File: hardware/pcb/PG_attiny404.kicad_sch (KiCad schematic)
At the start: 31 parts, among them J1 0022232041, J2 Conn_01x01_Male, J3 Conn_01x01_Male, J4 Conn_01x01_Male, J5 Conn_01x01_Male, J6 Conn_01x01_Male, J7 Conn_01x01_Male, J8 Conn_01x01_Male, J9 Conn_01x01_Male, Q1 2N7002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

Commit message: New PCB Version 0.1
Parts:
- removed C6: 100nF, Capacitor_SMD:C_0805_2012Metric_Pad1.18x1.45mm_HandSolder, symbol Device:C
- removed U2: AH9246, Package_TO_SOT_SMD:SC-59_Handsoldering, symbol project:AH9246
- added F1: 0ZCG0075FF2C, 0ZCG0075FF2C:0ZCG0075FF2C, symbol Device:Polyfuse
- added R7: 10k, Resistor_SMD:R_0805_2012Metric_Pad1.20x1.40mm_HandSolder, symbol Device:R
- added SW2: PTS526 SM15 SMTR2 LFS, PTS526_SK15_SMTR2_LFS:PTS526SK15SMTR2 LFS-M, symbol PTS526_SK15_SMTR2_LFS:PTS526_SM15_SMTR2_LFS
- added TVS1: SMF13A, SMF13A:SMFSeries_LTF, symbol SMF13A:SMF13A
- added TVS2, TVS3, TVS4: ESDA041-1JY, ESDA041-1JY:CR_041-1JY_STM, symbol ESDA041-1JY:ESDA041-1JY
- J1: footprint SOT23:PinHeader_1x04_P2.54mm_Horizontal_spezial -> digikey-footprints:PinHeader_1x4_P2.54mm_Drill1.02mm; DK_Detail_Page https://www.digikey.at/de/products/detail/molex/0022286040/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 -> /product-detail/en/molex/0022232041/WM4202-ND/26671; Description_1 (none) -> CONN HEADER VERT 4POS 2.54MM
- J2, J3, J4, J5, J6, J7, J8, J9: symbol Connector:Conn_01x01_Male -> Connector:Conn_01x01_Pin
- MOSFET1: footprint SOT23:SOT-23F_TOS-L -> SOT23:SOT-23F_TOS
- Q1: value 2N7002 -> 2N7002K-AU_R1_000A2; footprint Package_TO_SOT_SMD:SOT-323_SC-70_Handsoldering -> Package_TO_SOT_SMD:SOT-23_Handsoldering; symbol PG_attiny404-rescue:2N7002-dk_Transistors-FETs-MOSFETs-Single -> PG_attiny804:2N7002-dk_Transistors-FETs-MOSFETs-Single; DK_Detail_Page https://www.digikey.at/de/products/detail/panjit-internatio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 -> https://www.digikey.at/en/products/detail/panjit-internatio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; Description_1 (none) -> MOSFET N-CH 60V 115MA SOT-23
- R1: value 68 Ohm -> 62 Ohm
- R2: value 68 Ohm -> 100 Ohm
- U1: value ATtiny404-SS -> ATtiny804-SS; symbol PG_attiny404-rescue:ATtiny404-SS-MCU_Microchip_ATtiny -> PG_attiny804:ATtiny404-SS-MCU_Microchip_ATtiny
- U4: footprint Package_TO_SOT_SMD:SC-59_Handsoldering -> Package_TO_SOT_SMD:SOT-23_Handsoldering
- U5: footprint Package_TO_SOT_SMD:SOT-89-3_Handsoldering -> Package_TO_SOT_SMD:SOT-89-3
- U6: footprint Package_TO_SOT_SMD:SOT-23-6_Handsoldering -> Package_TO_SOT_SMD:SOT-23-6; symbol project:MP6513GJ -> PG_attiny804:MP6513GJ
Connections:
- net +3V3: now also SW2.2, TVS3.2
- net +BATT: now also TVS1.2 (K)
- net GND: now also R7.2, TVS1.1 (A), TVS2.1, TVS3.1, TVS4.1
- net Hall: now also R7.1, SW2.4
- net Soilmoisture: now also TVS2.2
- net at J5.1 (Pin_1), Q1.3 (D): now also TVS4.2
- net at J3.1 (Pin_1): now also F1.1; no longer MOSFET1.3
- new net: F1.2, MOSFET1.3
- no-connect marks 0 -> 2
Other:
- moved on the sheet: MOSFET1

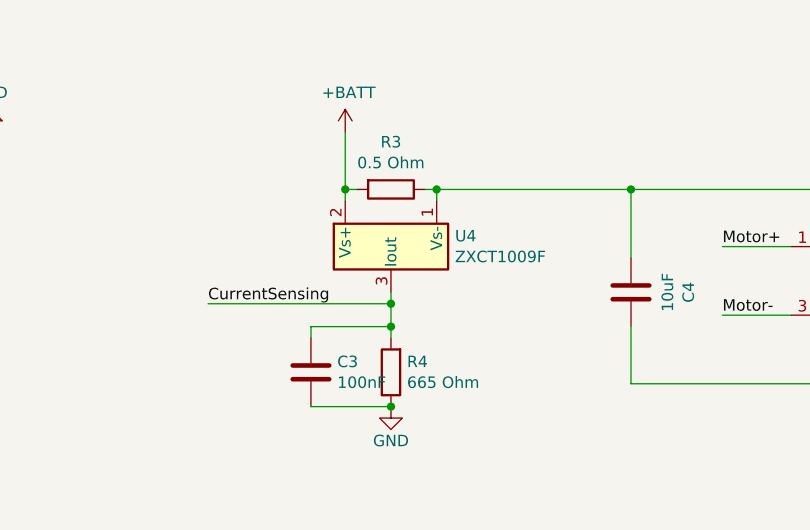
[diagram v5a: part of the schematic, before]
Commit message: Footprint correction for Current Sensor
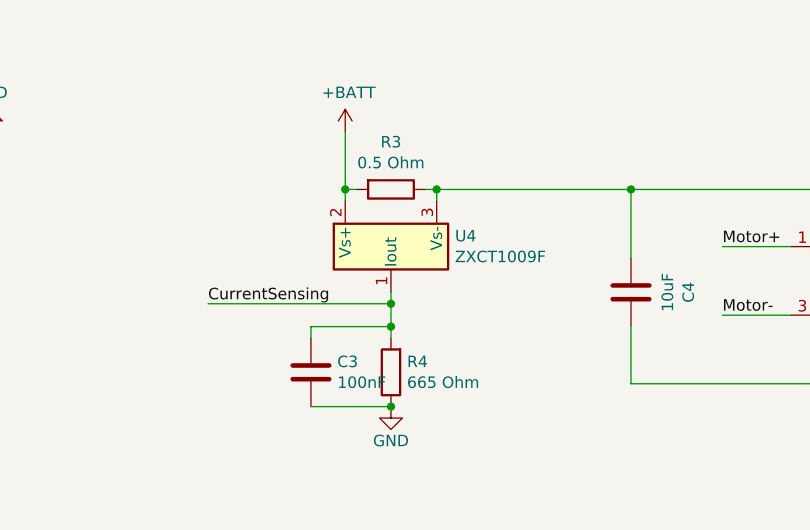
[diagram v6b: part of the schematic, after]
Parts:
- U4: footprint Package_TO_SOT_SMD:SOT-23_Handsoldering -> ZXCT1009F:SOT-23_Handsoldering_ZXCT1009F; symbol Amplifier_Current:ZXCT1009F -> ZXCT1009F:ZXCT1009F
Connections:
- net CurrentSensing: now also U4.1 (Iout); no longer U4.3 (Iout)
- net at C4.2, R3.1, U6.5 (VCC): now also U4.3 (Vs-); no longer U4.1 (Vs-)
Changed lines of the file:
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@@
 	)
 	(symbol
-		(lib_id "Amplifier_Current:ZXCT1009F")
+		(lib_id "ZXCT1009F:ZXCT1009F")
 		(at 184.15 48.26 0)
 		(unit 1)
@@
 			)
 		)
-		(property "Footprint" "Package_TO_SOT_SMD:SOT-23_Handsoldering"
+		(property "Footprint" "ZXCT1009F:SOT-23_Handsoldering_ZXCT1009F"
 			(at 184.15 48.26 0)
 			(effects

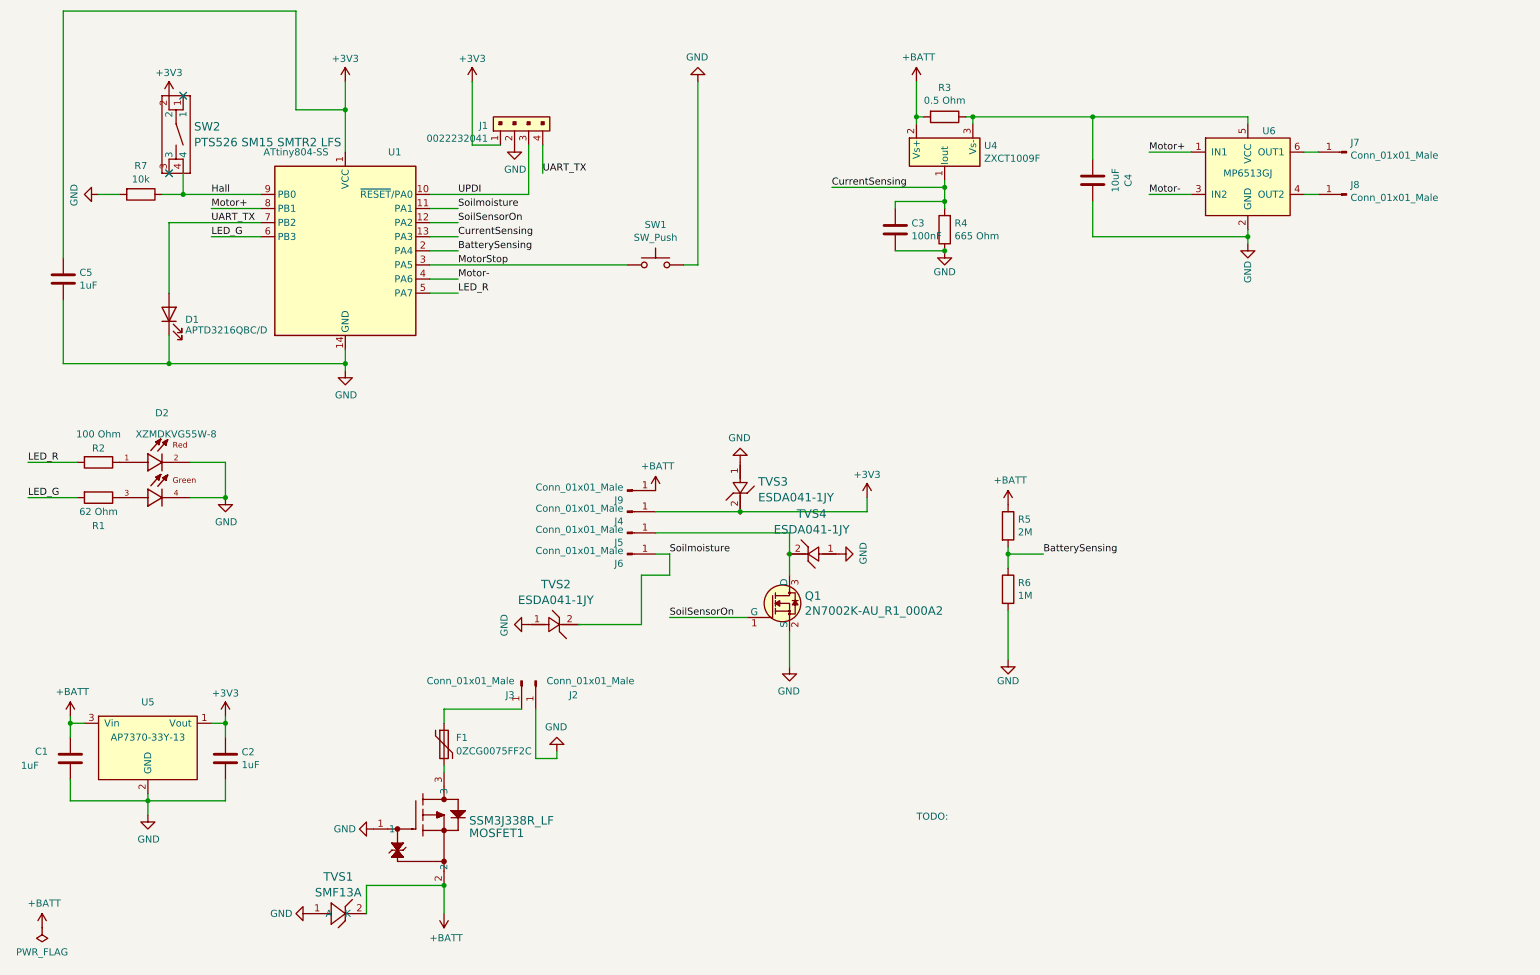
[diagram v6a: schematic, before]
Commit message: Added new motor driver to pcb
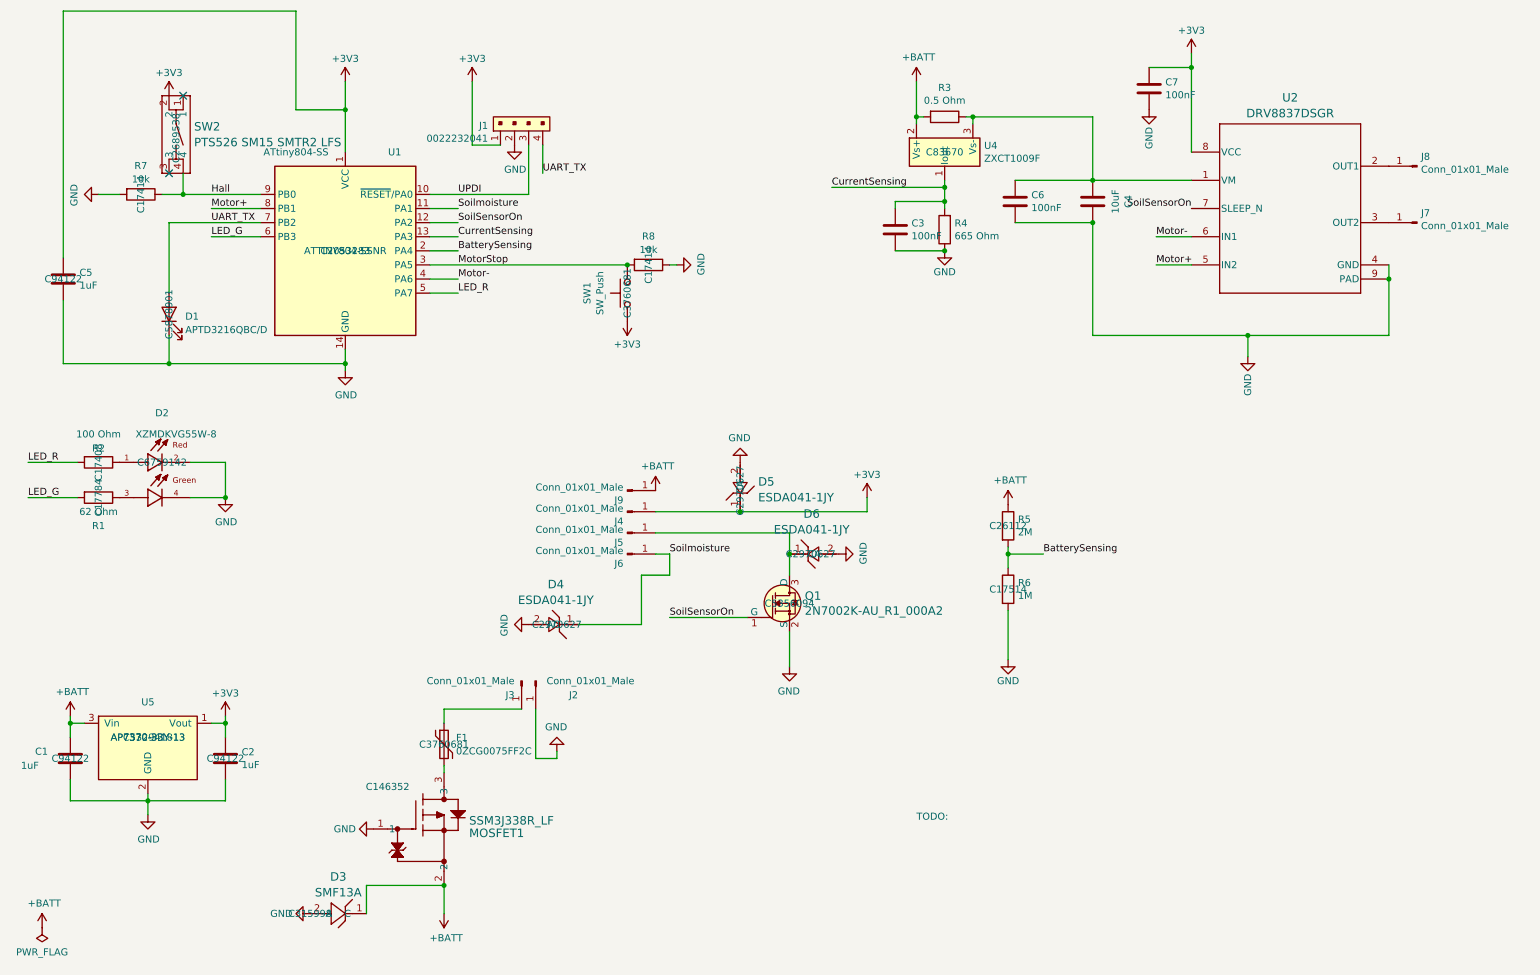
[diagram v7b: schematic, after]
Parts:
- removed U6: MP6513GJ, Package_TO_SOT_SMD:SOT-23-6, symbol PG_attiny804:MP6513GJ
- added C6, C7: 100nF, Capacitor_SMD:C_0805_2012Metric_Pad1.18x1.45mm_HandSolder, symbol Device:C
- added R8: 10k, Resistor_SMD:R_0805_2012Metric_Pad1.20x1.40mm_HandSolder, symbol Device:R
- added U2: DRV8837DSGR, DRV8837DSGR:DRV8837DSGR_NV, symbol DRV8837DSGR:DRV8837DSGR
- C1, C2, C5: JLC (none) -> C94122; MPN (none) -> CL21B105KOFNNNE
- C3: JLC (none) -> C519980; MPN (none) -> CC0805KRX7R7BB104
- C4: JLC (none) -> C326595; MPN (none) -> CL21A106KOQNNNG
- D1: JLC (none) -> C5878901; MPN (none) -> APTD3216QBC/D
- D2: JLC (none) -> C6759142; MPN (none) -> XZMDKVG55W-8
- D3: renamed from TVS1; JLC (none) -> C315998; MPN (none) -> SMF13A; Manufacturer (none) -> Littelfuse
- D4: renamed from TVS2; JLC (none) -> C2970627; MPN (none) -> ESDA041-1JY
- D5: renamed from TVS3; JLC (none) -> C2970627; MPN (none) -> ESDA041-1JY
- D6: renamed from TVS4; JLC (none) -> C2970627; MPN (none) -> ESDA041-1JY
- F1: JLC (none) -> C3760681; MPN (none) -> 0ZCG0075FF2C; Manufacturer (none) -> Bel Fuse Inc.
- J1: DK_Detail_Page /product-detail/en/molex/0022232041/WM4202-ND/26671 -> https://www.digikey.at/de/products/detail/molex/0022286040/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; MPN 0022232041 -> 0022286040; now left out of the parts list
- J2, J3, J4, J5, J6, J7, J8, J9: now left out of the parts list
- MOSFET1: JLC (none) -> C146352; MPN (none) -> SSM3J338R,LF
- Q1: JLC (none) -> C5356094; MPN 2N7002 -> 2N7002K-AU_R1_000A2
- R1: DK_Detail_Page https://www.digikey.at/de/products/detail/stackpole-electro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 -> https://www.digikey.at/en/products/detail/stackpole-electro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; JLC (none) -> C17784; MPN (none) -> RMCF0805FT62R0
- R2: DK_Detail_Page https://www.digikey.at/de/products/detail/stackpole-electro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 -> https://www.digikey.at/en/products/detail/stackpole-electro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; JLC (none) -> C17408; MPN (none) -> RMCF0805FT100R
- R3: JLC (none) -> C859814; MPN (none) -> RL1220S-R50-F
- R4: JLC (none) -> C17798; MPN (none) -> CRGCQ0805F680R
- R5: JLC (none) -> C26112; MPN (none) -> RMCF0805FT2M00
- R6: JLC (none) -> C17514; MPN (none) -> RMCF0805FG1M00
- R7: JLC (none) -> C17414; MPN (none) -> ERJ-6GEYJ103V
- SW1: JLC (none) -> C3760681; MPN (none) -> 1825027-2
- SW2: JLC (none) -> C2689538; MPN (none) -> PTS526SM15SMTR2 LFS; now in the parts list
- U1: JLC (none) -> C2053283; MPN (none) -> ATTINY804-SSNR
- U4: JLC (none) -> C83670; MPN (none) -> ZXCT1009FTA
- U5: JLC (none) -> C5329418; MPN (none) -> AP7370-33Y-13
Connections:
- net +3V3: now also D5.1 (C), SW1.2, C7.2, U2.8 (VCC); no longer D5.2
- net +BATT: now also D3.1 (C); no longer D3.2 (K)
- net GND: now also D3.2 (A), D4.2 (A), D5.2 (A), D6.2 (A), C6.1, C7.1, R8.1, U2.4 (GND), U2.9 (PAD); no longer D3.1 (A), D4.1, D5.1, D6.1, SW1.1
- net Motor+: now also U2.5 (IN2)
- net Motor-: now also U2.6 (IN1)
- net MotorStop: now also SW1.1, R8.2; no longer SW1.2
- net SoilSensorOn: now also U2.7 (SLEEP_N)
- net Soilmoisture: now also D4.1 (C); no longer D4.2
- net at C4.2, R3.1, U4.3 (Vs-): now also C6.2, U2.1 (VM)
- net at J8.1 (Pin_1): now also U2.2 (OUT1)
- net at J5.1 (Pin_1), Q1.3 (D): now also D6.1 (C); no longer D6.2
- net at J7.1 (Pin_1): now also U2.3 (OUT2)
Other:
- moved on the sheet: C4, J7, J8, SW1

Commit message: Small Changes for Ordering PCB
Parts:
- added J10: Cap +, digikey-footprints:PROBE_PAD_0603, symbol Connector:Conn_01x01_Pin
- added J11: Cap -, digikey-footprints:PROBE_PAD_0603, symbol Connector:Conn_01x01_Pin
- MOSFET1: FT Rotation Offset (none) -> 90
- R8: value 10k -> 220k; DK_Detail_Page https://www.digikey.at/de/products/detail/panasonic-electro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 -> https://www.digikey.at/de/products/detail/te-connectivity-p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; JLC C17414 -> C17556; MPN ERJ-6GEYJ103V -> CRG0805F220K
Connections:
- net GND: now also J11.1 (Pin_1)
- net at C4.2, C6.2, R3.1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: now also J10.1 (Pin_1)
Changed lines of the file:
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@@
 	)
 	(junction
+		(at 210.82 81.28)
+		(diameter 0)
+		(color 0 0 0 0)
+	)
+	(junction
 		(at 228.6 33.02)
 		(diameter 0)
@@
 	)
 	(junction
+		(at 210.82 41.91)
+		(diameter 0)
+		(color 0 0 0 0)
+	)
+	(junction
 		(at 184.15 66.04)
 		(diameter 0)
@@
 	(wire
 		(pts
+			(xy 179.07 35.56) (xy 179.07 41.91)
+		)
+		(stroke
+			(width 0)
+			(type default)
+		)
+	)
+	(wire
+		(pts
 			(xy 132.08 120.65) (xy 134.62 120.65)
 		)
@@
 	(wire
 		(pts
-			(xy 179.07 41.91) (xy 179.07 35.56)
-		)
-		(stroke
-			(width 0)
-			(type default)
-		)
-	)
-	(wire
-		(pts
 			(xy 238.76 81.28) (xy 264.16 81.28)
 		)
@@
 		(fields_autoplaced yes)
 		(property "Reference" "R8"
-			(at 130.81 63.4195 90)
+			(at 130.81 62.23 90)
 			(effects
 				(font
@@
 			)
 		)
-		(property "Value" "10k"
-			(at 130.81 65.8438 90)
+		(property "Value" "220k"
+			(at 130.81 64.77 90)
 			(effects
 				(font
@@
 			)
 		)
-		(property "DK_Detail_Page" "https://www.digikey.at/de/products/detail/panasonic-electronic-components/ERJ-6GEYJ103V/83062"
+		(property "DK_Detail_Page" "https://www.digikey.at/de/products/detail/te-connectivity-passive-product/CRG0805F220K/2380869"
 			(at 130.81 68.58 0)
 			(effects
@@
 			)
 		)
-		(property "MPN" "ERJ-6GEYJ103V"
+		(property "MPN" "CRG0805F220K"
 			(at 130.81 68.58 0)
 			(effects
@@
 			)
 		)
-		(property "JLC" "C17414"
+		(property "JLC" "C17556"
 			(at 130.81 68.58 0)
 			(effects
@@
 					(size 1.27 1.27)
 				)
+				(hide yes)
 			)
 		)
@@
 	)
 	(symbol
+		(lib_id "Connector:Conn_01x01_Pin")
+		(at 210.82 36.83 270)
+		(unit 1)
+		(exclude_from_sim no)
+		(in_bom no)
+		(on_board yes)
+		(dnp no)
+		(property "Reference" "J10"
+			(at 209.0928 36.1188 0)
+			(effects
+				(font
+					(size 1.27 1.27)
+				)
+				(justify right)
+			)
+		)
+		(property "Value" "Cap +"
+			(at 211.4042 36.1188 0)
+			(effects
+				(font
+					(size 1.27 1.27)
+				)
+				(justify right)
+			)
+		)
+		(property "Footprint" "digikey-footprints:PROBE_PAD_0603"
+			(at 210.82 36.83 0)
+			(effects
+				(font
+					(size 1.27 1.27)
+				)
+				(hide yes)
+			)
+		)
+		(property "Datasheet" "~"
+			(at 210.82 36.83 0)
+			(effects
+				(font
+					(size 1.27 1.27)
+				)
+				(hide yes)
+			)
+		)
+		(property "Description" "Generic connector, single row, 01x01, script generated"
+			(at 210.82 36.83 0)
+			(effects
+				(font
+					(size 1.27 1.27)
+				)
+				(hide yes)
+			)
+		)
+		(property "Manufacturer" ""
+			(at 210.82 36.83 0)
+			(effects
+				(font
+					(size 1.27 1.27)
+				)
+			)
+		)
+		(pin "1"
+		)
+		(instances
+			(project "PG_attiny404"
+				(path "/e68a78e5-8846-4666-9105-5fa8784d19c8"
+					(reference "J10")
+					(unit 1)
+				)
+			)
+		)
+	)
+	(symbol
 		(lib_id "Device:Polyfuse")
 		(at 93.98 154.94 0)
@@
 	)
 	(symbol
+		(lib_id "Connector:Conn_01x01_Pin")
+		(at 205.74 81.28 0)
+		(unit 1)
+		(exclude_from_sim no)
+		(in_bom no)
+		(on_board yes)
+		(dnp no)
+		(property "Reference" "J11"
+			(at 205.0288 83.0072 0)
+			(effects
+				(font
+					(size 1.27 1.27)
+				)
+				(justify right)
+			)
+		)
+		(property "Value" "Cap -"
+			(at 205.0288 80.6958 0)
+			(effects
+				(font
+					(size 1.27 1.27)
+				)
+				(justify right)
+			)
+		)
+		(property "Footprint" "digikey-footprints:PROBE_PAD_0603"
+			(at 205.74 81.28 0)
+			(effects
+				(font
+					(size 1.27 1.27)
+				)
+				(hide yes)
+			)
+		)
+		(property "Datasheet" "~"
+			(at 205.74 81.28 0)
+			(effects
+				(font
+					(size 1.27 1.27)
+				)
+				(hide yes)
+			)
+		)
+		(property "Description" "Generic connector, single row, 01x01, script generated"
+			(at 205.74 81.28 0)
+			(effects
+				(font
+					(size 1.27 1.27)
+				)
+				(hide yes)
+			)
+		)
+		(property "Manufacturer" ""
+			(at 205.74 81.28 0)
+			(effects
+				(font
+					(size 1.27 1.27)
+				)
+			)
+		)
+		(pin "1"
+		)
+		(instances
+			(project "PG_attiny404"
+				(path "/e68a78e5-8846-4666-9105-5fa8784d19c8"
+					(reference "J11")
+					(unit 1)
+				)
+			)
+		)
+	)
+	(symbol
 		(lib_id "PTS526_SK15_SMTR2_LFS:PTS526_SM15_SMTR2_LFS")
 		(at 45.72 45.72 270)
@@
 			)
 		)
+		(property "FT Rotation Offset" "90"
+			(at 83.82 162.56 0)
+			(effects
+				(font
+					(size 1.27 1.27)
+				)
+				(hide yes)
+			)
+		)
